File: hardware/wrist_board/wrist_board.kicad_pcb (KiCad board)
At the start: 4 copper layers, 60 x 42 mm, 56 parts, among them J1 S2B-PH-K-S_LF__SN_, J2 USB_C_Receptacle_USB2.0_14P, J3 Conn_01x02, J4 Conn_01x02, J5 Conn_01x02, J6 Conn_01x02, J7 Conn_01x02, J8 GPIOs, SW1 SW_SPST, U1 MCP73831T-2ACI_OT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

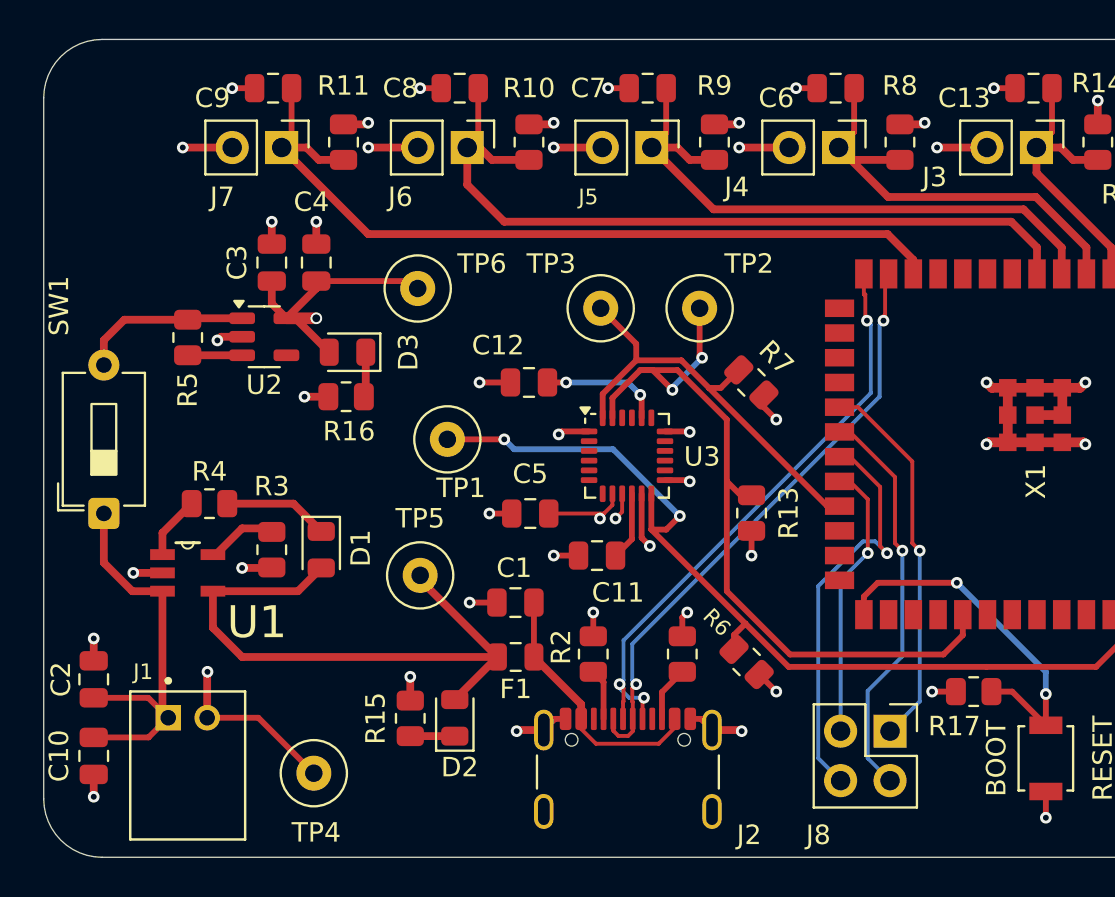
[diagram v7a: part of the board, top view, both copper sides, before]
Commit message: Updated silkscreen and fills
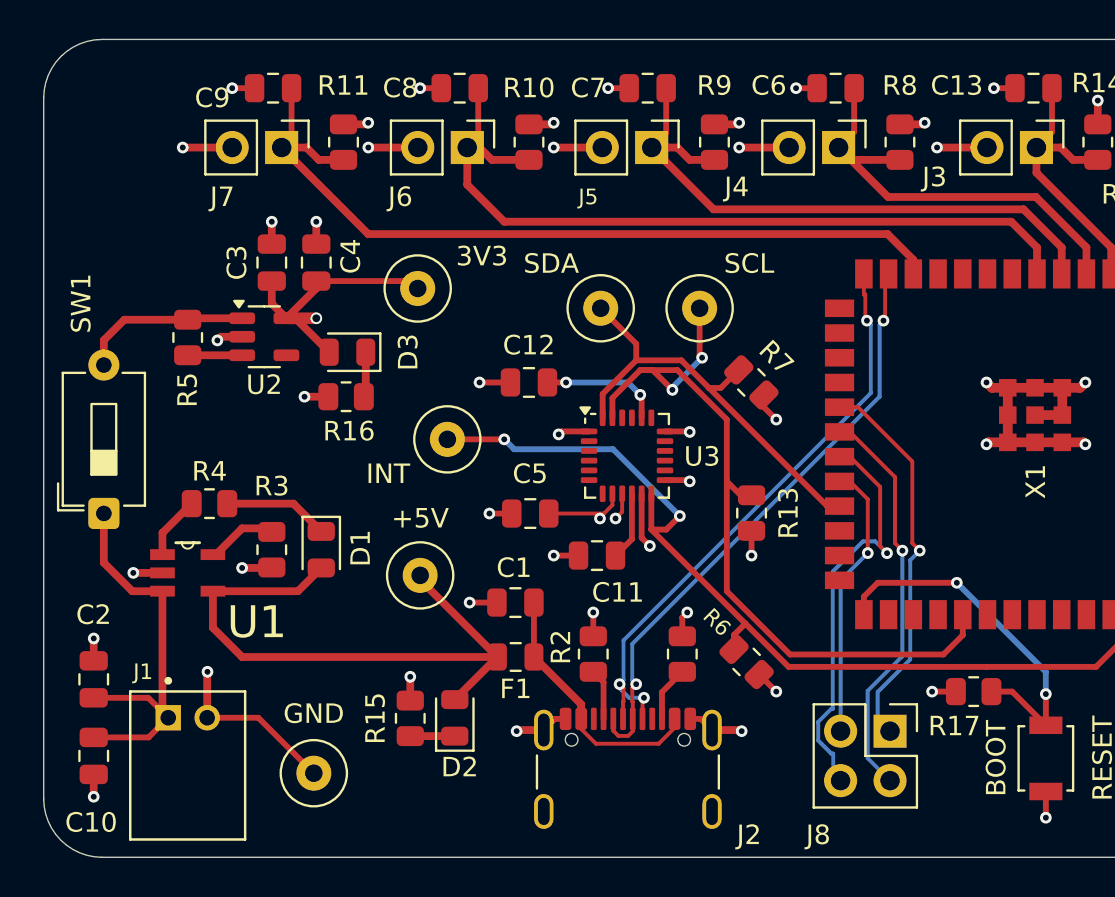
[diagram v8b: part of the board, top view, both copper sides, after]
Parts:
- renumbered TP5 to +5V, TP6 to 3V3, TP4 to GND, TP1 to INT, TP2 to SCL, TP3 to SDA
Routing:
- net /IO11: track 19.5 -> 20.1 mm
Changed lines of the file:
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@@
 		(descr "wire loop with bead as test point, loop diameter2.6mm, hole diameter 0.9mm")
 		(tags "test point wire loop bead")
-		(property "Reference" "TP5"
+		(property "Reference" "+5V"
 			(at 0 -2.921 0)
 			(layer "F.SilkS")
@@
 		(descr "wire loop with bead as test point, loop diameter2.6mm, hole diameter 0.9mm")
 		(tags "test point wire loop bead")
-		(property "Reference" "TP1"
-			(at 0.7 2.5 0)
+		(property "Reference" "INT"
+			(at -3.048 1.778 0)
 			(layer "F.SilkS")
 			(effects
@@
 			(layer "F.Fab")
 		)
-		(fp_text user "${REFERENCE}"
-			(at 0.7 2.5 0)
-			(layer "F.Fab")
-			(effects
-				(font
-					(size 1 1)
-					(thickness 0.15)
-				)
-			)
-		)
 		(pad "1" thru_hole circle
 			(at 0 0)
@@
 		(tags "capacitor")
 		(property "Reference" "C2"
-			(at 0 -1.68 90)
+			(at 3.307 0 180)
 			(layer "F.SilkS")
 			(effects
@@
 		(descr "wire loop with bead as test point, loop diameter2.6mm, hole diameter 0.9mm")
 		(tags "test point wire loop bead")
-		(property "Reference" "TP2"
+		(property "Reference" "SCL"
 			(at 2.54 -2.286 0)
 			(layer "F.SilkS")
@@
 			)
 		)
-		(fp_text user "${REFERENCE}"
-			(at 0 0 0)
-			(unlocked yes)
-			(layer "F.Fab")
-			(effects
-				(font
-					(size 1 1)
-					(thickness 0.15)
-				)
-			)
-		)
 		(pad "" np_thru_hole circle
 			(at -2.89 -2.605)
@@
 		(tags "capacitor")
 		(property "Reference" "C4"
-			(at 3.114 -0.254 180)
+			(at 0.32 1.778 270)
 			(layer "F.SilkS")
 			(effects
@@
 		(descr "wire loop with bead as test point, loop diameter2.6mm, hole diameter 0.9mm")
 		(tags "test point wire loop bead")
-		(property "Reference" "TP3"
+		(property "Reference" "SDA"
 			(at -2.54 -2.286 0)
 			(layer "F.SilkS")
@@
 		(descr "wire loop with bead as test point, loop diameter2.6mm, hole diameter 0.9mm")
 		(tags "test point wire loop bead")
-		(property "Reference" "TP6"
-			(at 3.302 -1.27 0)
+		(property "Reference" "3V3"
+			(at 3.302 -1.651 0)
 			(layer "F.SilkS")
 			(effects
@@
 		(tags "DIP Switch SPST Slide 7.62mm 300mil LowProfile")
 		(property "Reference" "SW1"
-			(at 10.663 -2.2985 90)
+			(at 10.79 -1.1555 90)
 			(layer "F.SilkS")
 			(effects
@@
 		(tags "capacitor")
 		(property "Reference" "C10"
-			(at 0 1.778 90)
+			(at 3.429 0.127 180)
 			(layer "F.SilkS")
 			(effects
@@
 		(tags "capacitor")
 		(property "Reference" "C12"
-			(at 1.59 1.905 0)
+			(at 0 1.905 0)
 			(layer "F.SilkS")
 			(effects
@@
 		(descr "wire loop with bead as test point, loop diameter2.6mm, hole diameter 0.9mm")
 		(tags "test point wire loop bead")
-		(property "Reference" "TP4"
-			(at 0.127 3.048 0)
+		(property "Reference" "GND"
+			(at 0 -3.048 0)
 			(layer "F.SilkS")
 			(effects
@@
 		(tags "capacitor")
 		(property "Reference" "C13"
-			(at 3.556 -0.508 0)
+			(at 3.937 0.127 0)
 			(layer "F.SilkS")
 			(effects
@@
 		(tags "capacitor")
 		(property "Reference" "C6"
-			(at 3.048 -0.508 0)
+			(at 3.429 0.127 0)
 			(layer "F.SilkS")
 			(effects
@@
 	)
 	(segment
-		(start 109.222362 111.667)
-		(end 108.590057 111.667)
+		(start 108.590056 111.667)
+		(end 107.061 113.196056)
+		(width 0.2)
+		(layer "B.Cu")
+		(net 39)
+	)
+	(segment
+		(start 107.061 113.196056)
+		(end 107.061 113.4789)
 		(width 0.2)
 		(layer "B.Cu")
@@
 	)
 	(segment
-		(start 108.590057 111.667)
-		(end 106.291 113.966057)
+		(start 109.827882 112.27252)
+		(end 109.222362 111.667)
 		(width 0.2)
 		(layer "B.Cu")
@@
 	)
 	(segment
-		(start 106.291 122.801)
+		(start 107.061 123.571)
 		(end 107.442 123.952)
 		(width 0.2)
@@
 	)
 	(segment
-		(start 106.291 113.966057)
-		(end 106.291 122.801)
+		(start 107.061 113.4789)
+		(end 107.041 113.4989)
 		(width 0.2)
 		(layer "B.Cu")
@@
 	)
 	(segment
-		(start 109.827882 112.27252)
-		(end 109.222362 111.667)
+		(start 109.222362 111.667)
+		(end 108.590056 111.667)
+		(width 0.2)
+		(layer "B.Cu")
+		(net 39)
+	)
+	(segment
+		(start 106.96524 122.563)
+		(end 107.061 122.563)
+		(width 0.2)
+		(layer "B.Cu")
+		(net 39)
+	)
+	(segment
+		(start 107.041 120.261)
+		(end 106.96524 120.261)
+		(width 0.2)
+		(layer "B.Cu")
+		(net 39)
+	)
+	(segment
+		(start 106.291 121.88876)
+		(end 106.96524 122.563)
+		(width 0.2)
+		(layer "B.Cu")
+		(net 39)
+	)
+	(segment
+		(start 106.291 120.93524)
+		(end 106.291 121.88876)
+		(width 0.2)
+		(layer "B.Cu")
+		(net 39)
+	)
+	(segment
+		(start 107.061 122.563)
+		(end 107.061 123.571)
+		(width 0.2)
+		(layer "B.Cu")
+		(net 39)
+	)
+	(segment
+		(start 106.96524 120.261)
+		(end 106.291 120.93524)
+		(width 0.2)
+		(layer "B.Cu")
+		(net 39)
+	)
+	(segment
+		(start 107.041 113.4989)
+		(end 107.041 120.261)
 		(width 0.2)
 		(layer "B.Cu")
@@
 	)
 	(segment
-		(start 108.831 119.34876)
-		(end 108.831 122.801)
-		(width 0.2)
-		(layer "B.Cu")
-		(net 40)
-	)
-	(segment
 		(start 110.617 112.141)
 		(end 110.617 117.56276)
@@
 	)
 	(segment
+		(start 108.831 119.34876)
+		(end 108.831 122.801)
+		(width 0.2)
+		(layer "B.Cu")
+		(net 40)
+	)
+	(segment
 		(start 108.712 98.981)
 		(end 108.638 98.981)
@@
 	)
 	(segment
-		(start 111.506 119.888)
+		(start 109.347 120.777)
 		(end 109.982 121.412)
 		(width 0.2)
@@
 	)
 	(segment
+		(start 109.347 119.39986)
+		(end 109.347 120.777)
+		(width 0.2)
+		(layer "B.Cu")
+		(net 54)
+	)
+	(segment
 		(start 111.506 112.141)
-		(end 111.506 119.888)
+		(end 111.018 112.629)
+		(width 0.2)
+		(layer "B.Cu")
+		(net 54)
+	)
+	(segment
+		(start 111.018 112.629)
+		(end 111.018 117.72886)
+		(width 0.2)
+		(layer "B.Cu")
+		(net 54)
+	)
+	(segment
+		(start 111.018 117.72886)
+		(end 109.347 119.39986)
 		(width 0.2)
 		(layer "B.Cu")
@@
 		(polygon
 			(pts
-				(xy 65.2272 127.9652) (xy 64.8208 86.9696) (xy 126.5428 87.122) (xy 126.492 127.4064)
+				(xy 65.405 128.397) (xy 64.77 80.899) (xy 126.619 80.518) (xy 126.492 128.651)
 			)
 		)
@@
 		(polygon
 			(pts
-				(xy 65.2272 127.9652) (xy 64.8208 86.9696) (xy 126.5428 87.122) (xy 126.492 127.4064)
+				(xy 65.278 128.397) (xy 64.8462 80.899) (xy 126.619 80.518) (xy 126.5682 128.651)
 			)
 		)
